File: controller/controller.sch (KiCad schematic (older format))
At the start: 22 parts, among them J1 PowerIN, J2 DebugInterface, J3 Screw_Terminal_01x04, J4 LockTerminal, Q1 PBSS4540, U1 LM317, U2 STM32F030K6Tx

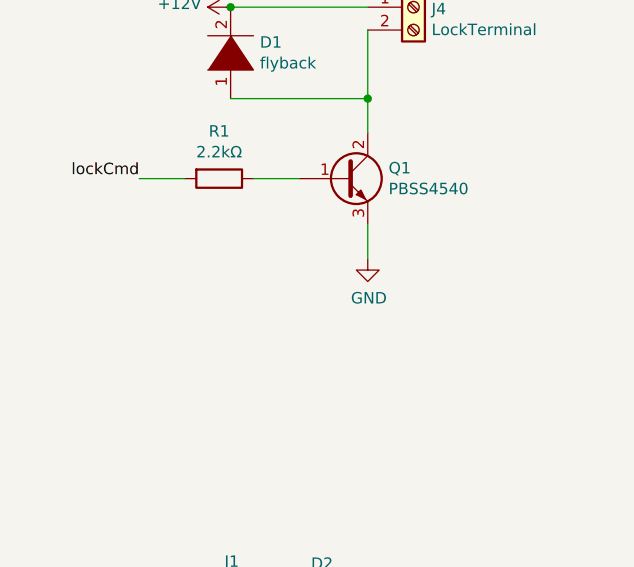
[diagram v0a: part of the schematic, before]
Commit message: adding current sensing
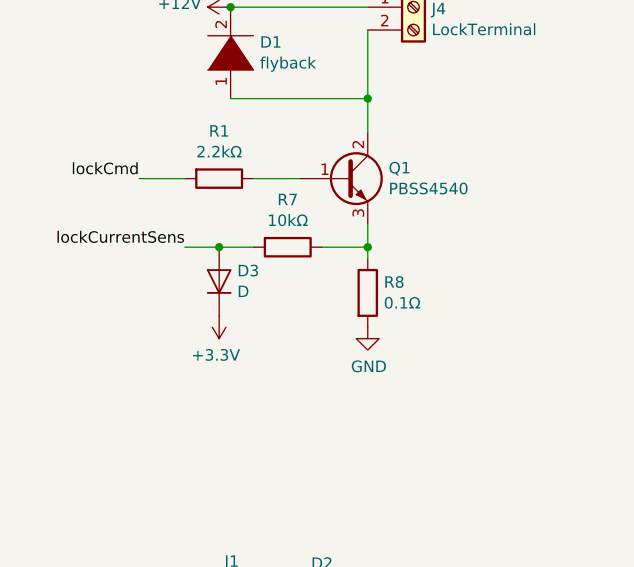
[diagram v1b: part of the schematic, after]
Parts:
- added D3: D, symbol Device:D
- added R7: 10kΩ, symbol Device:R
- added R8: 0.1Ω, symbol Device:R
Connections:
- net +3V3: now also D3.1 (K)
- net GND: now also R8.2; no longer Q1.3 (E)
- new net: Q1.3 (E), R7.1, R8.1
- new net lockCurrentSens: D3.2 (A), R7.2
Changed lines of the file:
@@
 	1950 1250 1950 1400
 Connection ~ 1950 1250
-Wire Wire Line
-	1950 1800 1950 1950
-$Comp
-L power:GND #PWR05
-U 1 1 5BDADE4C
-P 1950 1950
-F 0 "#PWR05" H 1950 1700 50  0001 C CNN
-F 1 "GND" H 1955 1777 50  0000 C CNN
-F 2 "" H 1950 1950 50  0001 C CNN
-F 3 "" H 1950 1950 50  0001 C CNN
-	1    1950 1950
-	1    0    0    -1
-$EndComp
 Text Label 950  1600 2    50   ~ 0
 lockCmd
@@
 Wire Wire Line
 	6400 3550 6800 3550
+$Comp
+L Device:R R8
+U 1 1 5BF53F47
+P 1950 2100
+F 0 "R8" H 2020 2146 50  0000 L CNN
+F 1 "0.1Ω" H 2020 2055 50  0000 L CNN
+F 2 "" V 1880 2100 50  0001 C CNN
+F 3 "~" H 1950 2100 50  0001 C CNN
+	1    1950 2100
+	1    0    0    -1
+$EndComp
+$Comp
+L power:GND #PWR016
+U 1 1 5BF53FD1
+P 1950 2250
+F 0 "#PWR016" H 1950 2000 50  0001 C CNN
+F 1 "GND" H 1955 2077 50  0000 C CNN
+F 2 "" H 1950 2250 50  0001 C CNN
+F 3 "" H 1950 2250 50  0001 C CNN
+	1    1950 2250
+	1    0    0    -1
+$EndComp
+$Comp
+L Device:R R7
+U 1 1 5BF54A94
+P 1600 1900
+F 0 "R7" V 1393 1900 50  0000 C CNN
+F 1 "10kΩ" V 1484 1900 50  0000 C CNN
+F 2 "" V 1530 1900 50  0001 C CNN
+F 3 "~" H 1600 1900 50  0001 C CNN
+	1    1600 1900
+	0    1    1    0
+$EndComp
+$Comp
+L Device:D D3
+U 1 1 5BF54BFC
+P 1300 2050
+F 0 "D3" V 1346 1971 50  0000 R CNN
+F 1 "D" V 1255 1971 50  0000 R CNN
+F 2 "" H 1300 2050 50  0001 C CNN
+F 3 "~" H 1300 2050 50  0001 C CNN
+	1    1300 2050
+	0    -1   -1   0
+$EndComp
+$Comp
+L power:+3.3V #PWR05
+U 1 1 5BF54DDB
+P 1300 2200
+F 0 "#PWR05" H 1300 2050 50  0001 C CNN
+F 1 "+3.3V" H 1315 2373 50  0000 C CNN
+F 2 "" H 1300 2200 50  0001 C CNN
+F 3 "" H 1300 2200 50  0001 C CNN
+	1    1300 2200
+	-1   0    0    1
+$EndComp
+Text Label 1150 1900 2    50   ~ 0
+lockCurrentSens
+Wire Wire Line
+	1150 1900 1300 1900
+Wire Wire Line
+	1950 1800 1950 1900
+Wire Wire Line
+	1750 1900 1950 1900
+Connection ~ 1950 1900
+Wire Wire Line
+	1950 1900 1950 1950
+Wire Wire Line
+	1300 1900 1450 1900
+Connection ~ 1300 1900
 $EndSCHEMATC
